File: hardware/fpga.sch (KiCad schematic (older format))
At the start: 61 parts, among them CON1 SD_Card_DM3BT, P10 CONN_01X01, P11 CONN_01X01, P12 CONN_01X01, P13 CONN_01X01, P14 CONN_01X01, P15 CONN_01X01, P16 CONN_01X01, P3 CONN_02X04, P4 CONN_02X04, P6 CONN_01X01, P9 CONN_01X01, Q2 DNP(RE1C002UN), SW1 DNP, SW2 SW_PUSH, U30 XC7A15T-1FTG256C, U40 W25Q32JV

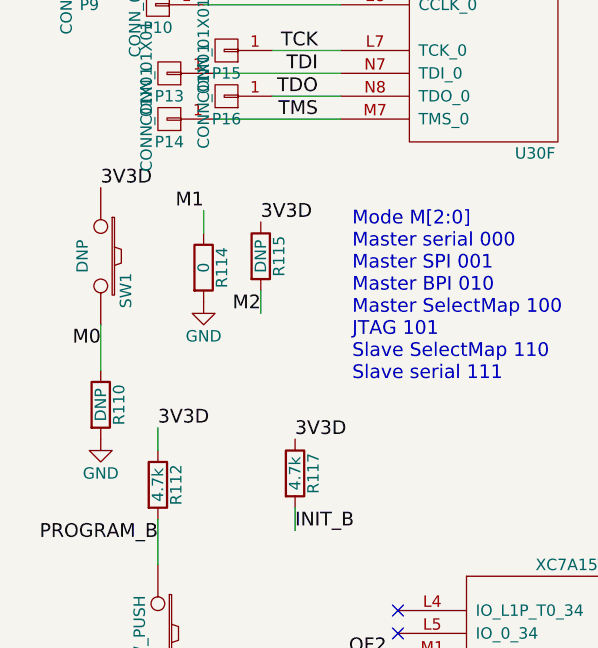
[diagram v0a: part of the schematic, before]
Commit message: Fix FPGA programming resistor connections
M[2:0] were wired incorrectly when I ordered the board. For programming from SPI
memory M[2:0] should be "001", but I had them wired backwards as "100". I fixed
it with one jump wire, but here is a proper fix for anyone looking to reproduce
the design.
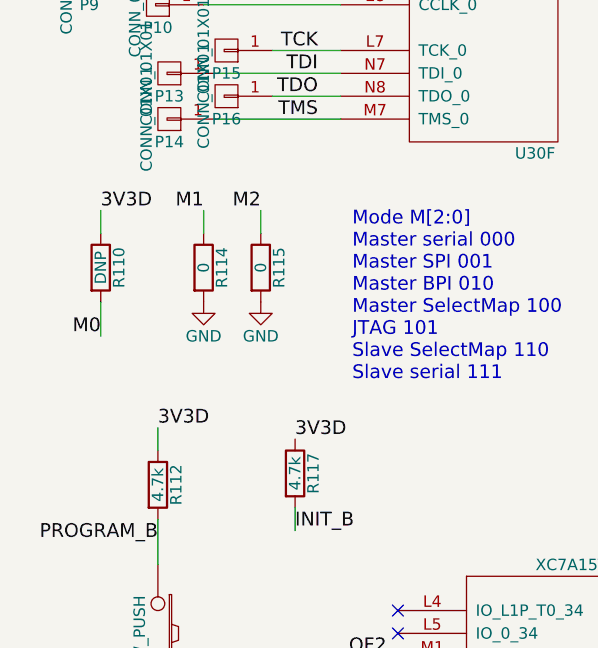
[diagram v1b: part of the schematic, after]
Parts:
- removed SW1: DNP, fmcw3:EVP-AWBA2A, symbol SW_PUSH
- R115: value DNP -> 0
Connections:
- net 3V3D: now also R110.1; no longer R115.1
- net GND: now also R115.2; no longer R110.2
- net M0: now also R110.2; no longer R110.1
- net M2: now also R115.1; no longer R115.2
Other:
- moved on the sheet: R110, R115
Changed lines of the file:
@@
 	900  5950 1800 5950
-$Comp
-L SW_PUSH SW1
-U 1 1 585531EB
-P 750 7150
-F 0 "SW1" H 900 7260 50  0000 C CNN
-F 1 "DNP" H 750 7070 50  0000 C CNN
-F 2 "fmcw3:EVP-AWBA2A" H 750 7150 60  0001 C CNN
-F 3 "" H 750 7150 60  0000 C CNN
-	1    750  7150
-	0    1    1    0
-$EndComp
 $Comp
 L R R114
@@
 L R R115
 U 1 1 58553EF2
-P 1450 7150
-F 0 "R115" V 1530 7150 50  0000 C CNN
-F 1 "DNP" V 1450 7150 50  0000 C CNN
-F 2 "fmcw3:R_0402b" V 1380 7150 30  0001 C CNN
-F 3 "" H 1450 7150 30  0000 C CNN
-	1    1450 7150
+P 1450 7200
+F 0 "R115" V 1530 7200 50  0000 C CNN
+F 1 "0" V 1450 7200 50  0000 C CNN
+F 2 "fmcw3:R_0402b" V 1380 7200 30  0001 C CNN
+F 3 "" H 1450 7200 30  0000 C CNN
+	1    1450 7200
 	1    0    0    -1
 $EndComp
@@
 	1    0    0    -1
 $EndComp
-Text Label 1450 7000 0    60   ~ 0
-3V3D
 Wire Wire Line
 	1200 6950 1200 7050
-Wire Wire Line
-	1450 7300 1450 7400
 $Comp
 L R R110
 U 1 1 5855502E
-P 750 7800
-F 0 "R110" V 830 7800 50  0000 C CNN
-F 1 "DNP" V 750 7800 50  0000 C CNN
-F 2 "fmcw3:R_0402b" V 680 7800 30  0001 C CNN
-F 3 "" H 750 7800 30  0000 C CNN
-	1    750  7800
-	1    0    0    -1
-$EndComp
-$Comp
-L GND #PWR025
-U 1 1 58555513
-P 750 7950
-F 0 "#PWR025" H 750 7700 50  0001 C CNN
-F 1 "GND" H 750 7800 50  0000 C CNN
-F 2 "" H 750 7950 60  0000 C CNN
-F 3 "" H 750 7950 60  0000 C CNN
-	1    750  7950
-	1    0    0    -1
-$EndComp
-Wire Wire Line
-	750  7450 750  7650
-Text Label 750  6850 0    60   ~ 0
+P 750 7200
+F 0 "R110" V 830 7200 50  0000 C CNN
+F 1 "DNP" V 750 7200 50  0000 C CNN
+F 2 "fmcw3:R_0402b" V 680 7200 30  0001 C CNN
+F 3 "" H 750 7200 30  0000 C CNN
+	1    750  7200
+	1    0    0    -1
+$EndComp
+Text Label 750  6950 0    60   ~ 0
 3V3D
 $Comp
@@
 Text Notes 1850 7700 0    60   ~ 0
 Mode M[2:0]\nMaster serial 000\nMaster SPI 001\nMaster BPI 010\nMaster SelectMap 100\nJTAG 101\nSlave SelectMap 110\nSlave serial 111
-Text Label 750  7550 2    60   ~ 0
+Text Label 750  7500 2    60   ~ 0
 M0
 Text Label 1200 6950 2    60   ~ 0
 M1
-Text Label 1450 7400 2    60   ~ 0
+Text Label 1450 6950 2    60   ~ 0
 M2
 Text Label 1650 5750 2    60   ~ 0
@@
 Wire Wire Line
 	9050 1100 8550 1100
+$Comp
+L GND #PWR0255
+U 1 1 59CBD1DE
+P 1450 7350
+F 0 "#PWR0255" H 1450 7100 50  0001 C CNN
+F 1 "GND" H 1450 7200 50  0000 C CNN
+F 2 "" H 1450 7350 60  0000 C CNN
+F 3 "" H 1450 7350 60  0000 C CNN
+	1    1450 7350
+	1    0    0    -1
+$EndComp
+Wire Wire Line
+	1450 6950 1450 7050
+Wire Wire Line
+	750  7350 750  7500
+Wire Wire Line
+	750  7050 750  6950
 $EndSCHEMATC

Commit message: Update kicad:  * kicad_pcb from 20170123 to 20171130 (pcbnew from 75cda50 to 5ecfd32)  * EESchema from 2 to 4
fix pin 53 in U33 (remove path in pcb)
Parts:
- C170, C171, C174, C18, C183, C185, C186, C187, C188, C189, C190, C191, C192, C193, C194, C195, C197, C198, C199, C200, C201, C202, C203, C204, C205, C250, C251, C252: symbol C -> Device:C
- C181: footprint Capacitors_SMD:C_1210 -> Capacitor_SMD:C_1210_3225Metric; symbol C -> Device:C
- C182, C184, C196: footprint Capacitors_SMD:C_1206 -> Capacitor_SMD:C_1206_3216Metric; symbol C -> Device:C
- CON1: symbol SD_Card_DM3BT -> fmcw3:SD_Card_DM3BT
- D6: symbol LED -> Device:LED_ALT
- P10, P11, P12, P13, P14, P15, P16, P6, P9: value CONN_01X01 -> Conn_01x01; symbol CONN_01X01 -> Connector_Generic:Conn_01x01
- P3, P4: value CONN_02X04 -> Conn_02x04_Odd_Even; footprint Pin_Headers:Pin_Header_Straight_2x04_Pitch2.54mm_SMD -> Connector_PinHeader_2.54mm:PinHeader_2x04_P2.54mm_Vertical_SMD; symbol CONN_02X04 -> Connector_Generic:Conn_02x04_Odd_Even
- Q2: symbol MOS_N_GSD -> fmcw3:MOS_N_GSD
- R109, R110, R111, R112, R114, R115, R117, R118, R130, R69, R70: symbol R -> Device:R
- SW2: value SW_PUSH -> SW_Push; symbol SW_PUSH -> Switch:SW_Push
- U30: symbol XC7A15T-1FTG256C -> fmcw3:XC7A15T-1FTG256C
- U40: footprint Housings_DFN_QFN:DFN-S-8-1EP_6x5mm_Pitch1.27mm -> Package_DFN_QFN:DFN-S-8-1EP_6x5mm_P1.27mm; symbol W25Q32JV -> fmcw3:W25Q32JV
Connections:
- wire segments 332 -> 441
